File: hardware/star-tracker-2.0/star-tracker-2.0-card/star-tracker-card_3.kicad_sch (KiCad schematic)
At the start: 40 parts, among them J5 DM3BT-DSF-PEJS, U11 ICM-42688-P, U12 TCAN330, U13 EMMC+RESET+5.1-COMPATIBLE-BA, U7 OSD3358-512M-BSM

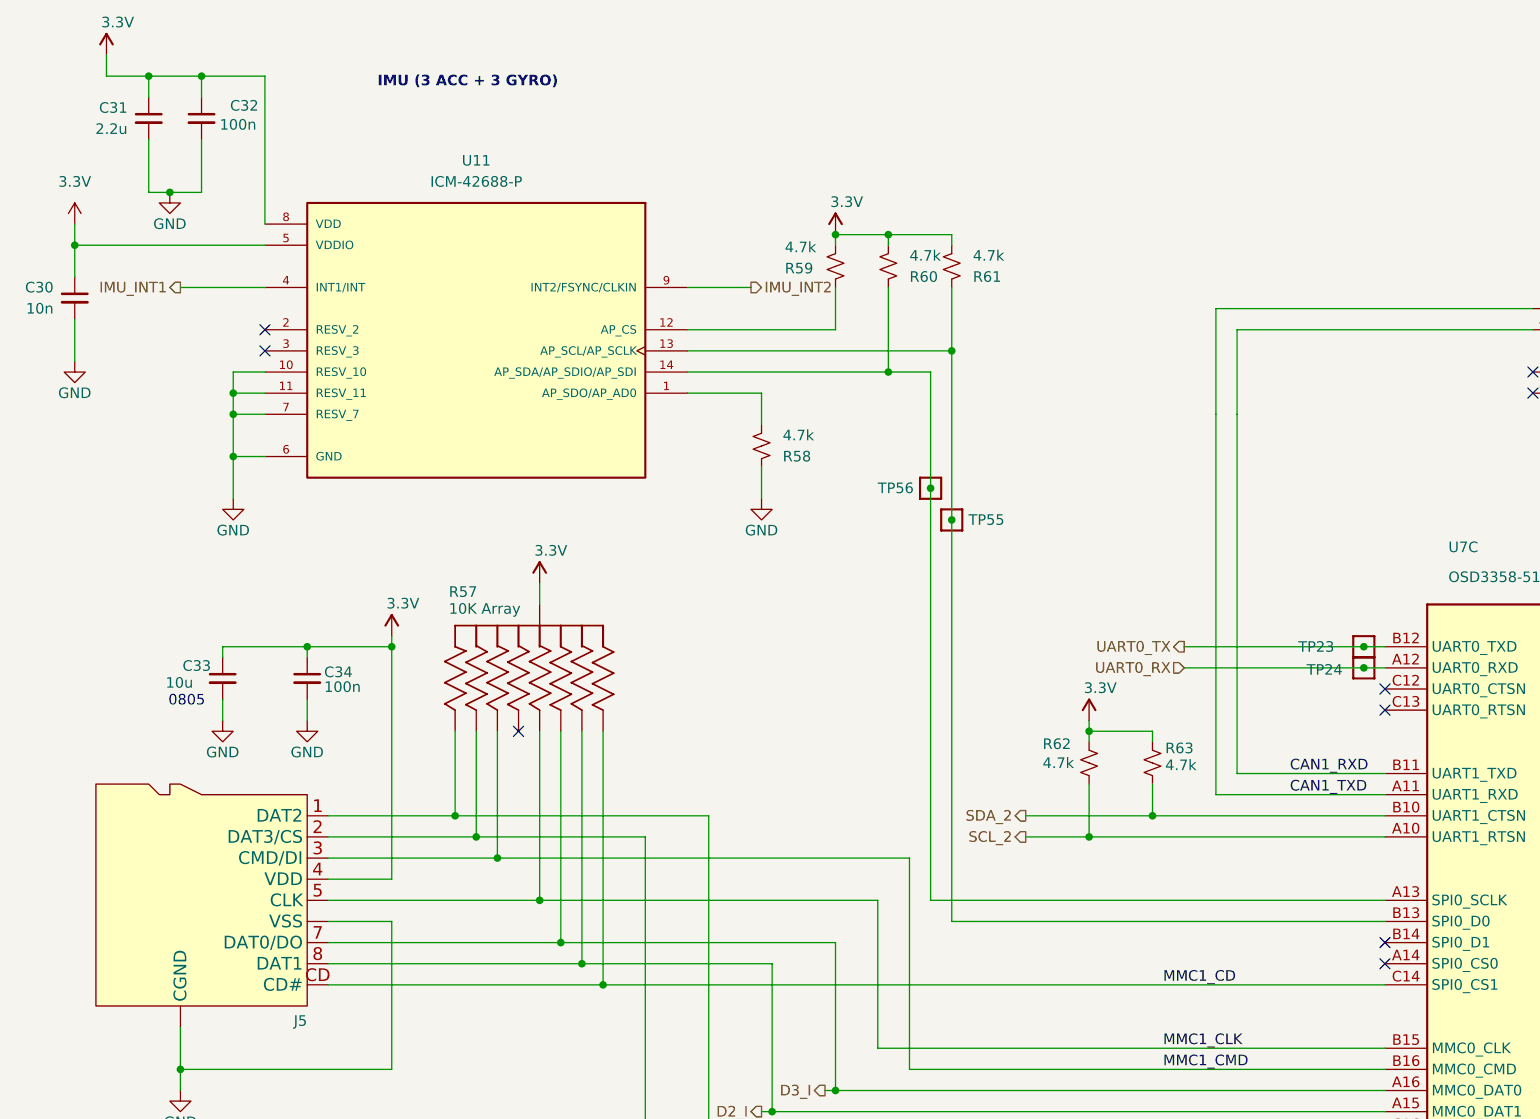
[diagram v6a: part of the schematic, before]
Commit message: Update
changed IMU to I2C bus 1, instead of shared bus 2 with the i2c camera control. Updated IMU interrupt pin location.
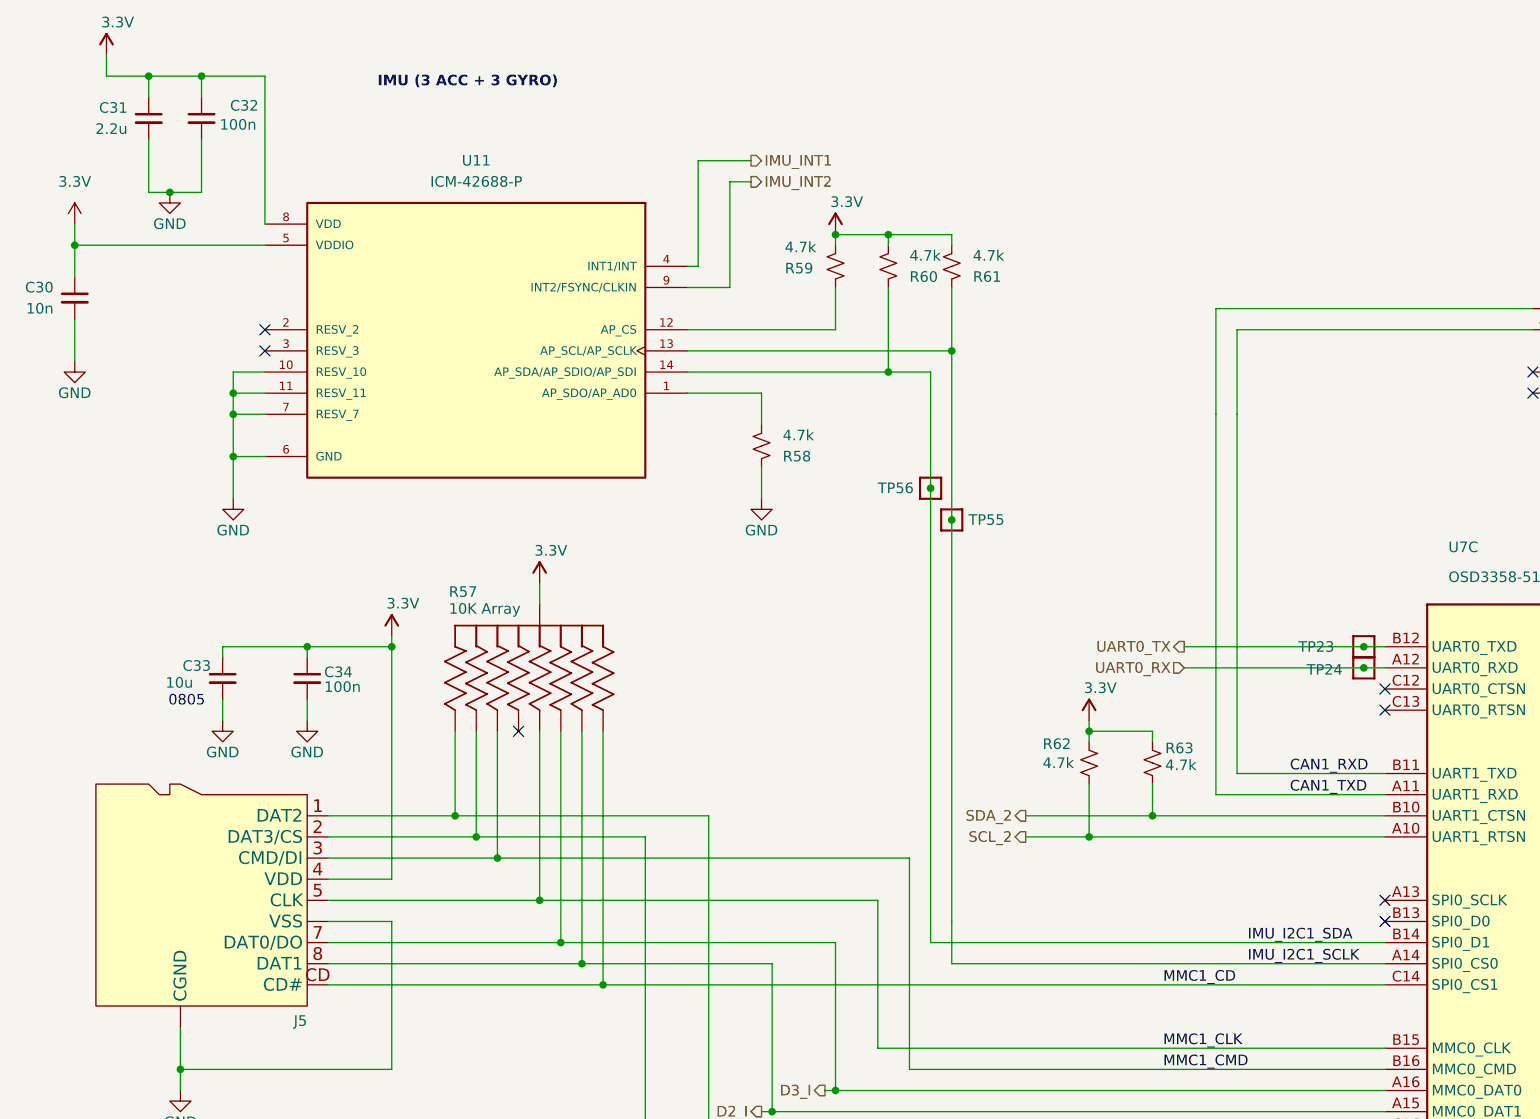
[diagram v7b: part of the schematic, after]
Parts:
- U11: MANUFACTURER (none) -> TDK InvenSense; MAXIMUM_PACKAGE_HEIGHT (none) -> 0.97mm; PARTREV (none) -> 1.2
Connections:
- net IMU_I2C1_SDA: now reaches R60.1, TP56.1, U11.14 (AP_SDA/AP_SDIO/AP_SDI)
- net IMU_I2C1_SDA: now also U7.B14 (SPI0_D1); no longer U7.A13 (SPI0_SCLK)
- net IMU_I2C1_SCLK: now reaches U7.A14 (SPI0_CS0)
- net IMU_I2C1_SCLK: now also R61.1, TP55.1, U11.13 (AP_SCL/AP_SCLK)
- now unconnected: U7.B13 (SPI0_D0)
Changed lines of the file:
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@@
 	)
 	(no_connect
+		(at 186.69 146.05)
+	)
+	(no_connect
 		(at 52.07 74.93)
 	)
@@
 	)
 	(no_connect
+		(at 186.69 143.51)
+	)
+	(no_connect
 		(at 247.65 168.91)
 	)
@@
 	)
 	(no_connect
-		(at 186.69 151.13)
-	)
-	(no_connect
 		(at 247.65 204.47)
 	)
@@
 	)
 	(no_connect
-		(at 186.69 148.59)
-	)
-	(no_connect
 		(at 247.65 146.05)
 	)
@@
 	(wire
 		(pts
-			(xy 134.62 146.05) (xy 186.69 146.05)
-		)
-		(stroke
-			(width 0.1524)
-			(type solid)
-		)
-	)
-	(wire
-		(pts
 			(xy 247.65 133.35) (xy 262.89 133.35)
 		)
@@
 	(wire
 		(pts
+			(xy 104.14 54.61) (xy 104.14 67.31)
+		)
+		(stroke
+			(width 0)
+			(type default)
+		)
+	)
+	(wire
+		(pts
 			(xy 361.95 158.75) (xy 361.95 161.29)
 		)
@@
 	(wire
 		(pts
-			(xy 102.87 69.85) (xy 110.49 69.85)
+			(xy 134.62 151.13) (xy 186.69 151.13)
+		)
+		(stroke
+			(width 0)
+			(type default)
+		)
+	)
+	(wire
+		(pts
+			(xy 107.95 57.15) (xy 110.49 57.15)
 		)
 		(stroke
@@
 	(wire
 		(pts
+			(xy 107.95 57.15) (xy 107.95 69.85)
+		)
+		(stroke
+			(width 0)
+			(type default)
+		)
+	)
+	(wire
+		(pts
 			(xy 283.21 128.27) (xy 285.75 128.27)
 		)
@@
 	(wire
 		(pts
-			(xy 41.91 69.85) (xy 52.07 69.85)
+			(xy 334.01 201.93) (xy 323.85 201.93)
 		)
 		(stroke
-			(width 0)
-			(type default)
+			(width 0.1524)
+			(type solid)
 		)
 	)
 	(wire
 		(pts
-			(xy 334.01 201.93) (xy 323.85 201.93)
+			(xy 186.69 199.39) (xy 167.64 199.39)
 		)
 		(stroke
@@
 	(wire
 		(pts
-			(xy 186.69 199.39) (xy 167.64 199.39)
+			(xy 52.07 62.23) (xy 52.07 44.45)
 		)
 		(stroke
-			(width 0.1524)
-			(type solid)
+			(width 0)
+			(type default)
 		)
 	)
 	(wire
 		(pts
-			(xy 52.07 62.23) (xy 52.07 44.45)
+			(xy 186.69 148.59) (xy 132.08 148.59)
 		)
 		(stroke
@@
 	(wire
 		(pts
+			(xy 134.62 151.13) (xy 134.62 146.05)
+		)
+		(stroke
+			(width 0)
+			(type default)
+		)
+	)
+	(wire
+		(pts
 			(xy 57.15 113.03) (xy 67.31 113.03)
 		)
@@
 	(wire
 		(pts
+			(xy 107.95 69.85) (xy 102.87 69.85)
+		)
+		(stroke
+			(width 0)
+			(type default)
+		)
+	)
+	(wire
+		(pts
 			(xy 377.19 148.59) (xy 346.71 148.59)
 		)
@@
 	(wire
 		(pts
+			(xy 132.08 148.59) (xy 132.08 143.51)
+		)
+		(stroke
+			(width 0)
+			(type default)
+		)
+	)
+	(wire
+		(pts
 			(xy 334.01 199.39) (xy 328.93 199.39)
 		)
@@
 	(wire
 		(pts
+			(xy 104.14 67.31) (xy 102.87 67.31)
+		)
+		(stroke
+			(width 0)
+			(type default)
+		)
+	)
+	(wire
+		(pts
 			(xy 334.01 196.85) (xy 326.39 196.85)
 		)
@@
 	(wire
 		(pts
-			(xy 132.08 143.51) (xy 186.69 143.51)
+			(xy 110.49 54.61) (xy 104.14 54.61)
 		)
 		(stroke
-			(width 0.1524)
-			(type solid)
+			(width 0)
+			(type default)
 		)
 	)
@@
 		)
 	)
+	(label "IMU_I2C1_SDA"
+		(at 170.18 148.59 0)
+		(effects
+			(font
+				(size 1.27 1.27)
+			)
+			(justify left bottom)
+		)
+	)
 	(label "EMMC_D0"
 		(at 269.24 173.99 0)
@@
 		)
 	)
+	(label "IMU_I2C1_SCLK"
+		(at 170.18 151.13 0)
+		(effects
+			(font
+				(size 1.27 1.27)
+			)
+			(justify left bottom)
+		)
+	)
 	(label "EMMC_D2"
 		(at 269.24 179.07 0)
@@
 		)
 	)
-	(hierarchical_label "IMU_INT1"
-		(shape output)
-		(at 41.91 69.85 180)
-		(effects
-			(font
-				(size 1.27 1.27)
-			)
-			(justify right)
-		)
-	)
 	(hierarchical_label "D4_I"
 		(shape output)
@@
 		)
 	)
+	(hierarchical_label "IMU_INT1"
+		(shape output)
+		(at 110.49 54.61 0)
+		(effects
+			(font
+				(size 1.27 1.27)
+			)
+			(justify left)
+		)
+	)
 	(hierarchical_label "IMU_INT2"
 		(shape output)
-		(at 110.49 69.85 0)
+		(at 110.49 57.15 0)
 		(effects
 			(font
@@
 			)
 		)
+		(property "PARTREV" "1.2"
+			(at 77.47 46.482 0)
+			(hide yes)
+			(show_name no)
+			(do_not_autoplace no)
+			(effects
+				(font
+					(size 1.27 1.27)
+				)
+				(justify bottom)
+			)
+		)
+		(property "MAXIMUM_PACKAGE_HEIGHT" "0.97mm"
+			(at 77.47 50.8 0)
+			(hide yes)
+			(show_name no)
+			(do_not_autoplace no)
+			(effects
+				(font
+					(size 1.27 1.27)
+				)
+				(justify bottom)
+			)
+		)
+		(property "MANUFACTURER" "TDK InvenSense"
+			(at 77.724 52.578 0)
+			(hide yes)
+			(show_name no)
+			(do_not_autoplace no)
+			(effects
+				(font
+					(size 1.27 1.27)
+				)
+				(justify bottom)
+			)
+		)
